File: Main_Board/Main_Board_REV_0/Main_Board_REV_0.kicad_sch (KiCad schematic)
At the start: 24 parts, among them J1 ERF6-30-03.5-L-DV-A-K-TR, J2 ERF6-30-03.5-L-DV-A-K-TR, J3 ERF6-30-03.5-L-DV-A-K-TR, J4 ERF6-30-03.5-L-DV-A-K-TR, J5 ERF6-30-03.5-L-DV-A-K-TR, J6 ERF6-30-03.5-L-DV-A-K-TR, J7 ERF6-30-03.5-L-DV-A-K-TR, J8 ERF6-30-03.5-L-DV-A-K-TR

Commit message: .
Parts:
- added J10, J11, J12, J13, J14, J15, J16, J9: ERF6-30-03.5-L-DV-A-K-TR, 0-lib:SAMTEC_ERF6-30-03.5-L-DV-A-K-TR, symbol 0-lib:ERF6-30-03.5-L-DV-A-K-TR
- H1, H10, H11, H12, H13, H14, H15, H16, H2, H3, H4, H5, H6, H7, H8, H9: footprint MountingHole:MountingHole_2.2mm_M2_DIN965_Pad -> 0-lib:insert
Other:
- note added: "Amplifiers"
- note added: "Cube_1"
- note added: "Cube_2"
- note added: "Cube_3"
- note added: "Cube_4"
- note added: "FARICH"
- note added: "Mounting Inserts"
- title: Fibers Main Board -> Fiber - Main Board
- moved on the sheet: H1, H10, H11, H12, H13, H14, H15, H16, H2, H3, H4, H5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

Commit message: .
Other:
- added sheet Microcontroller (Microcontroller.kicad_sch)
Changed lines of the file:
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@@
+		)
+	)
+	(sheet
+		(at 15.24 438.15)
+		(size 187.96 130.81)
+		(exclude_from_sim no)
+		(in_bom yes)
+		(on_board yes)
+		(dnp no)
+		(stroke
+			(width 1.27)
+			(type solid)
+		)
+		(fill
+			(color 0 0 0 0.0000)
+		)
+		(property "Sheetname" "Microcontroller"
+			(at 66.802 506.222 0)
+			(effects
+				(font
+					(size 7.62 7.62)
+					(thickness 1.524)
+					(bold yes)
+				)
+				(justify left bottom)
+			)
+		)
+		(property "Sheetfile" "Microcontroller.kicad_sch"
+			(at 15.24 569.5446 0)
+			(effects
+				(font
+					(size 1.27 1.27)
+				)
+				(justify left top)
+				(hide yes)
+			)
+		)
+		(instances
+			(project "Main_Board_REV_0"
+				(path "/7125c2d5-be96-492e-8b70-c56cceaf676d"
+					(page "2")
+				)
+			)
 		)
 	)

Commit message: .
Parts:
- added J17: 1778764, 0-lib:PHOENIX_1778764, symbol 0-lib:1778764
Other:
- removed sheet Microcontroller
- moved on the sheet: J1, J10, J11, J12, J13, J14, J15, J16, J2, J3, J4, J5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

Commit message: .
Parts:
- added C1, C10, C11, C12, C13, C14, C15, C16, C17, C18, C19, C2, C20, C3, C4, C5, C6, C7, C8, C9: 10uF, Capacitor_SMD:C_0805_2012Metric, symbol Device:C_Small
- added J18, J20, J21, J22: NCP1117LPST33T3G, Package_TO_SOT_SMD:SOT-223, symbol Connector:Conn_01x03_Pin
- added J19: Conn_02x16_Odd_Even, Connector_PinHeader_2.54mm:PinHeader_2x16_P2.54mm_Vertical, symbol Connector_Generic:Conn_02x16_Odd_Even
- added J23: Amphenol_132289, Connector_Coaxial:SMA_Amphenol_132289_EdgeMount, symbol Connector:Conn_Coaxial_Small
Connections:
- net GND: now also J1.01, J1.03, J1.04, J1.06, J1.08, J1.10, J1.12, J1.13, J1.43, J1.45, J1.50, J1.52, J1.54, J1.56, J1.57, J1.58, J1.59, J1.60, J10.03, J10.04, J10.07, J10.08, J10.11, J10.12, J10.15, J10.16, J10.19, J10.23, J10.24, J10.27, J10.28, J10.31, J10.32, J10.35, J10.36, J10.39, J11.03, J11.04, J11.07, J11.08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
- net Out_D6_Cube_2: now reaches J12.01
- net Out_C8_Cube_2: now reaches J12.02
- net Out_B8_Cube_2: now reaches J12.05
- net Out_D8_Cube_2: now reaches J12.06
- net Out_D7_Cube_2: now reaches J12.09
- net Out_A8_Cube_2: now reaches J12.10
- net Out_C6_Cube_2: now reaches J12.13
- net Out_B7_Cube_2: now reaches J12.14
- net Out_D5_Cube_2: now reaches J12.17
- net Out_C7_Cube_2: now reaches J12.18
- net Out_A7_Cube_2: now reaches J12.21
- net Out_H6_Cube_2: now reaches J12.22
- net Out_A6_Cube_2: now reaches J12.25
- net Out_B5_Cube_2: now reaches J12.26
- net Out_B6_Cube_2: now reaches J12.29
- net Out_B2_Cube_2: now reaches J12.30
- net Out_C5_Cube_2: now reaches J12.33
- net Out_C4_Cube_2: now reaches J12.34
- net Out_C2_Cube_2: now reaches J12.37
- net Out_C3_Cube_2: now reaches J12.38
- net Out_B4_Cube_2: now reaches J12.41
- net Out_A4_Cube_2: now reaches J12.42
- net 1V1_Cube_2: now reaches J12.43
- net 1V1_Cube_2: now also J11.43, J11.44, J11.47, J11.48, J11.51, J11.52, J11.55, J11.56, J12.44, J12.47, J12.48, J12.51, J12.52, J12.55, J12.56
- net Out_D3_Cube_2: now reaches J12.45
- net Out_B3_Cube_2: now reaches J12.46
- net Out_D2_Cube_2: now reaches J12.49
- net Out_A2_Cube_2: now reaches J12.50
- net Out_C1_Cube_2: now reaches J12.53
- net Out_A1_Cube_2: now reaches J12.54
- net Out_B1_Cube_2: now reaches J12.57
- net Out_A3_Cube_2: now reaches J12.58
- net Out_D1_Cube_2: now reaches J12.59
- net Out_D4_Cube_2: now reaches J12.60
- net Out_E8_Cube_1: now reaches J9.01
- net Out_E7_Cube_1: now reaches J9.02
- net Out_H7_Cube_1: now reaches J9.05
- net Out_H8_Cube_1: now reaches J9.06
- net Out_G8_Cube_1: now reaches J9.09
- net Out_F7_Cube_1: now reaches J9.10
- net Out_G7_Cube_1: now reaches J9.13
- net Out_F6_Cube_1: now reaches J9.14
- net Out_F8_Cube_1: now reaches J9.17
- net Out_F5_Cube_1: now reaches J9.18
- net Out_H5_Cube_1: now reaches J9.21
- net Out_E5_Cube_1: now reaches J9.22
- net Out_A5_Cube_1: now reaches J9.25
- net Out_G5_Cube_1: now reaches J9.26
- net Out_G2_Cube_1: now reaches J9.29
- net Out_G6_Cube_1: now reaches J9.30
- net Out_F3_Cube_1: now reaches J9.33
- net Out_E6_Cube_1: now reaches J9.34
- net Out_E4_Cube_1: now reaches J9.37
- net Out_E1_Cube_1: now reaches J9.38
- net Out_H3_Cube_1: now reaches J9.41
- net Out_F4_Cube_1: now reaches J9.42
- net 1V1_Cube_1: now reaches J9.43
- net 1V1_Cube_1: now also J10.43, J10.44, J10.47, J10.48, J10.51, J10.52, J10.55, J10.56, J9.44, J9.47, J9.48, J9.51, J9.52, J9.55, J9.56
- net Out_G4_Cube_1: now reaches J9.45
- net Out_E3_Cube_1: now reaches J9.46
- net Out_H1_Cube_1: now reaches J9.49
- net Out_E2_Cube_1: now reaches J9.50
- net Out_H2_Cube_1: now reaches J9.53
- net Out_G1_Cube_1: now reaches J9.54
- net Out_G3_Cube_1: now reaches J9.57
- net Out_F1_Cube_1: now reaches J9.58
- net Out_H4_Cube_1: now reaches J9.59
- net Out_F2_Cube_1: now reaches J9.60
- net Out_E8_Cube_5: now reaches J13.01
- net Out_E7_Cube_5: now reaches J13.02
- net Out_H7_Cube_5: now reaches J13.05
- net Out_H8_Cube_5: now reaches J13.06
- net Out_G8_Cube_5: now reaches J13.09
- net Out_F7_Cube_5: now reaches J13.10
- net Out_G7_Cube_5: now reaches J13.13
- net Out_F6_Cube_5: now reaches J13.14
- net Out_F8_Cube_5: now reaches J13.17
- net Out_F5_Cube_5: now reaches J13.18
- net Out_H5_Cube_5: now reaches J13.21
- net Out_E5_Cube_5: now reaches J13.22
- net Out_A5_Cube_5: now reaches J13.25
- net Out_G5_Cube_5: now reaches J13.26
- net Out_G2_Cube_5: now reaches J13.29
- net Out_G6_Cube_5: now reaches J13.30
- net Out_F3_Cube_5: now reaches J13.33
- net Out_E6_Cube_5: now reaches J13.34
- net Out_E4_Cube_5: now reaches J13.37
- net Out_E1_Cube_5: now reaches J13.38
- net Out_H3_Cube_5: now reaches J13.41
- net Out_F4_Cube_5: now reaches J13.42
- net 1V1_Cube_5: now reaches J13.43
- net 1V1_Cube_5: now also J13.44, J13.47, J13.48, J13.51, J13.52, J13.55, J13.56, J15.43, J15.44, J15.47, J15.48, J15.51, J15.52, J15.55, J15.56
- net Out_G4_Cube_5: now reaches J13.45
- net Out_E3_Cube_5: now reaches J13.46
- net Out_H1_Cube_5: now reaches J13.49
- net Out_E2_Cube_5: now reaches J13.50
- net Out_H2_Cube_5: now reaches J13.53
- net Out_G1_Cube_5: now reaches J13.54
- net Out_G3_Cube_5: now reaches J13.57
- net Out_F1_Cube_5: now reaches J13.58
- net Out_H4_Cube_5: now reaches J13.59
- net Out_F2_Cube_5: now reaches J13.60
- net 4->5V: now reaches J17.1
- net 4->5V: now also C11.2, C14.2, C16.2, C2.1, C3.1, C5.1, C7.1, C9.2, J18.3 (Pin_3), J19.1 (Pin_1), J19.2 (Pin_2), J20.3 (Pin_3), J21.3 (Pin_3), J22.3 (Pin_3)
- net at J2.06: now also J2.08, J2.10, J2.12, J2.14
- net Ch_61_A1: now reaches J2.13
- net Ch_63_A1: now reaches J2.15
- net Ch_55_A1: now reaches J2.17
- net Ch_57_A1: now reaches J2.19
- net Ch_59_A1: now reaches J2.20
- net Ch_47_A1: now reaches J2.21
- net Ch_51_A1: now reaches J2.22
- net Ch_53_A1: now reaches J2.23
- net Ch_49_A1: now reaches J2.24
- net Ch_37_A1: now reaches J2.25
- net Ch_45_A1: now reaches J2.26
- net Ch_43_A1: now reaches J2.27
- net Ch_41_A1: now reaches J2.28
- net Ch_27_A1: now reaches J2.29
- net Ch_39_A1: now reaches J2.30
- net Ch_33_A1: now reaches J2.31
- net Ch_35_A1: now reaches J2.32
- net Ch_17_A1: now reaches J2.33
- net Ch_31_A1: now reaches J2.34
- net Ch_23_A1: now reaches J2.35
- net Ch_29_A1: now reaches J2.36
- net Ch_11_A1: now reaches J2.37
- net Ch_25_A1: now reaches J2.38
- net Ch_15_A1: now reaches J2.39
- net Ch_21_A1: now reaches J2.40
- net Ch_07_A1: now reaches J2.41
- net Ch_19_A1: now reaches J2.42
- net Ch_09_A1: now reaches J2.43
- net Ch_13_A1: now reaches J2.44
- net Ch_01_A1: now reaches J2.45
- net Ch_05_A1: now reaches J2.46
- net Ch_03_A1: now reaches J2.47
- net 1V1_A1: now reaches J2.50
- net 1V1_A1: now also J1.05, J1.07, J1.09, J1.11, J2.52, J2.54, J2.56
- net HV_1-32_A1: now reaches J2.59
- net HV_1-32_A1: now also J19.32 (Pin_32)
- net at J8.06: now also J8.08, J8.10, J8.12, J8.14
- net Ch_61_A4: now reaches J8.13
- net Ch_63_A4: now reaches J8.15
- net Ch_55_A4: now reaches J8.17
- net Ch_57_A4: now reaches J8.19
- net Ch_59_A4: now reaches J8.20
- net Ch_47_A4: now reaches J8.21
- net Ch_51_A4: now reaches J8.22
- net Ch_53_A4: now reaches J8.23
- net Ch_49_A4: now reaches J8.24
- net Ch_37_A4: now reaches J8.25
- net Ch_45_A4: now reaches J8.26
- net Ch_43_A4: now reaches J8.27
- net Ch_41_A4: now reaches J8.28
- net Ch_27_A4: now reaches J8.29
- net Ch_39_A4: now reaches J8.30
- net Ch_33_A4: now reaches J8.31
- net Ch_35_A4: now reaches J8.32
- net Ch_17_A4: now reaches J8.33
- net Ch_31_A4: now reaches J8.34
- net Ch_23_A4: now reaches J8.35
- net Ch_29_A4: now reaches J8.36
- net Ch_11_A4: now reaches J8.37
- net Ch_25_A4: now reaches J8.38
- net Ch_15_A4: now reaches J8.39
- net Ch_21_A4: now reaches J8.40
- net Ch_07_A4: now reaches J8.41
- net Ch_19_A4: now reaches J8.42
- net Ch_09_A4: now reaches J8.43
- net Ch_13_A4: now reaches J8.44
- net Ch_01_A4: now reaches J8.45
- net Ch_05_A4: now reaches J8.46
- net Ch_03_A4: now reaches J8.47
- net 1V1_A4: now reaches J8.50
- net 1V1_A4: now also J7.05, J7.07, J7.09, J7.11, J8.52, J8.54, J8.56
- net HV_1-32_A4: now reaches J8.59
- net HV_1-32_A4: now also J19.26 (Pin_26)
- net at J4.06: now also J4.08, J4.10, J4.12, J4.14
- net Ch_61_A2: now reaches J4.13
- net Ch_63_A2: now reaches J4.15
- net Ch_55_A2: now reaches J4.17
- net Ch_57_A2: now reaches J4.19
- net Ch_59_A2: now reaches J4.20
- net Ch_47_A2: now reaches J4.21
- net Ch_51_A2: now reaches J4.22
- net Ch_53_A2: now reaches J4.23
- net Ch_49_A2: now reaches J4.24
- net Ch_37_A2: now reaches J4.25
- net Ch_45_A2: now reaches J4.26
- net Ch_43_A2: now reaches J4.27
- net Ch_41_A2: now reaches J4.28
- net Ch_27_A2: now reaches J4.29
- net Ch_39_A2: now reaches J4.30
- net Ch_33_A2: now reaches J4.31
- net Ch_35_A2: now reaches J4.32
- net Ch_17_A2: now reaches J4.33
- net Ch_31_A2: now reaches J4.34
- net Ch_23_A2: now reaches J4.35
- net Ch_29_A2: now reaches J4.36
- net Ch_11_A2: now reaches J4.37
- net Ch_25_A2: now reaches J4.38
- net Ch_15_A2: now reaches J4.39
- net Ch_21_A2: now reaches J4.40
- net Ch_07_A2: now reaches J4.41
- net Ch_19_A2: now reaches J4.42
- net Ch_09_A2: now reaches J4.43
- net Ch_13_A2: now reaches J4.44
- net Ch_01_A2: now reaches J4.45
- net Ch_05_A2: now reaches J4.46
- net Ch_03_A2: now reaches J4.47
- net 1V1_A2: now reaches J4.50
- net 1V1_A2: now also J3.05, J3.07, J3.09, J3.11, J4.52, J4.54, J4.56
- net HV_1-32_A2: now reaches J4.59
- net HV_1-32_A2: now also J19.30 (Pin_30)
- net HV_33-64_A2: now reaches J3.02
- net HV_33-64_A2: now also J19.20 (Pin_20)
- net Ch_62_A2: now reaches J3.14
- net Ch_60_A2: now reaches J3.15
- net Ch_64_A2: now reaches J3.16
- net Ch_54_A2: now reaches J3.17
- net Ch_56_A2: now reaches J3.18
- net Ch_48_A2: now reaches J3.19
- net Ch_58_A2: now reaches J3.20
- net Ch_44_A2: now reaches J3.21
- net Ch_50_A2: now reaches J3.22
- net Ch_40_A2: now reaches J3.23
- net Ch_52_A2: now reaches J3.24
- net Ch_36_A2: now reaches J3.25
- net Ch_42_A2: now reaches J3.26
- net Ch_34_A2: now reaches J3.27
- net Ch_46_A2: now reaches J3.28
- net Ch_30_A2: now reaches J3.29
- net Ch_32_A2: now reaches J3.30
- net Ch_26_A2: now reaches J3.31
- net Ch_38_A2: now reaches J3.32
- net Ch_24_A2: now reaches J3.33
- net Ch_22_A2: now reaches J3.34
- net Ch_20_A2: now reaches J3.35
- net Ch_28_A2: now reaches J3.36
- net Ch_16_A2: now reaches J3.37
- net Ch_12_A2: now reaches J3.38
- net Ch_14_A2: now reaches J3.39
- net Ch_18_A2: now reaches J3.40
- net Ch_08_A2: now reaches J3.41
- net Ch_06_A2: now reaches J3.42
- net Ch_10_A2: now reaches J3.44
- net Ch_02_A2: now reaches J3.46
- net +3.3_2V: now reaches J3.47
- net +3.3_2V: now also J3.49, J3.51, J3.53, J3.55, C15.1, C18.1, C6.1, J21.2 (Pin_2)
- net Ch_04_A2: now reaches J3.48
- net Out_D6_Cube_1: now reaches J10.01
- net Out_C8_Cube_1: now reaches J10.02
- net Out_B8_Cube_1: now reaches J10.05
- net Out_D8_Cube_1: now reaches J10.06
- net Out_D7_Cube_1: now reaches J10.09
- net Out_A8_Cube_1: now reaches J10.10
- net Out_C6_Cube_1: now reaches J10.13
- net Out_B7_Cube_1: now reaches J10.14
- net Out_D5_Cube_1: now reaches J10.17
- net Out_C7_Cube_1: now reaches J10.18
- net Out_A7_Cube_1: now reaches J10.21
- net Out_H6_Cube_1: now reaches J10.22
- net Out_A6_Cube_1: now reaches J10.25
- net Out_B5_Cube_1: now reaches J10.26
- net Out_B6_Cube_1: now reaches J10.29
- net Out_B2_Cube_1: now reaches J10.30
- net Out_C5_Cube_1: now reaches J10.33
- net Out_C4_Cube_1: now reaches J10.34
- net Out_C2_Cube_1: now reaches J10.37
- net Out_C3_Cube_1: now reaches J10.38
- net Out_B4_Cube_1: now reaches J10.41
- net Out_A4_Cube_1: now reaches J10.42
- net Out_D3_Cube_1: now reaches J10.45
- net Out_B3_Cube_1: now reaches J10.46
- net Out_D2_Cube_1: now reaches J10.49
- net Out_A2_Cube_1: now reaches J10.50
- net Out_C1_Cube_1: now reaches J10.53
- net Out_A1_Cube_1: now reaches J10.54
- net Out_B1_Cube_1: now reaches J10.57
- net Out_A3_Cube_1: now reaches J10.58
- net Out_D1_Cube_1: now reaches J10.59
- net Out_D4_Cube_1: now reaches J10.60
- net HV_33-64_A3: now reaches J5.02
- net HV_33-64_A3: now also J19.22 (Pin_22)
- net 1V1_A3: now reaches J5.05
- net 1V1_A3: now also J5.07, J5.09, J5.11, J6.50, J6.52, J6.54, J6.56
- net Ch_62_A3: now reaches J5.14
- net Ch_60_A3: now reaches J5.15
- net Ch_64_A3: now reaches J5.16
- net Ch_54_A3: now reaches J5.17
- net Ch_56_A3: now reaches J5.18
- net Ch_48_A3: now reaches J5.19
- net Ch_58_A3: now reaches J5.20
- net Ch_44_A3: now reaches J5.21
- net Ch_50_A3: now reaches J5.22
- net Ch_40_A3: now reaches J5.23
- net Ch_52_A3: now reaches J5.24
- net Ch_36_A3: now reaches J5.25
- net Ch_42_A3: now reaches J5.26
- net Ch_34_A3: now reaches J5.27
- net Ch_46_A3: now reaches J5.28
- net Ch_30_A3: now reaches J5.29
- net Ch_32_A3: now reaches J5.30
- net Ch_26_A3: now reaches J5.31
- net Ch_38_A3: now reaches J5.32
- net Ch_24_A3: now reaches J5.33
- net Ch_22_A3: now reaches J5.34
- net Ch_20_A3: now reaches J5.35
- net Ch_28_A3: now reaches J5.36
- net Ch_16_A3: now reaches J5.37
- net Ch_12_A3: now reaches J5.38
- net Ch_14_A3: now reaches J5.39
- net Ch_18_A3: now reaches J5.40
- net Ch_08_A3: now reaches J5.41
- net Ch_06_A3: now reaches J5.42
- net Ch_10_A3: now reaches J5.44
- net Ch_02_A3: now reaches J5.46
- net +3.3_3V: now reaches J5.47
- net +3.3_3V: now also J5.49, J5.51, J5.53, J5.55, C12.1, C19.1, C4.1, J20.2 (Pin_2)
- net Ch_04_A3: now reaches J5.48
- net Out_D6_Cube_5: now reaches J15.01
- net Out_C8_Cube_5: now reaches J15.02
- net Out_B8_Cube_5: now reaches J15.05
- net Out_D8_Cube_5: now reaches J15.06
- net Out_D7_Cube_5: now reaches J15.09
- net Out_A8_Cube_5: now reaches J15.10
- net Out_C6_Cube_5: now reaches J15.13
- net Out_B7_Cube_5: now reaches J15.14
- net Out_D5_Cube_5: now reaches J15.17
- net Out_C7_Cube_5: now reaches J15.18
- net Out_A7_Cube_5: now reaches J15.21
- net Out_H6_Cube_5: now reaches J15.22
- net Out_A6_Cube_5: now reaches J15.25
- net Out_B5_Cube_5: now reaches J15.26
- net Out_B6_Cube_5: now reaches J15.29
- net Out_B2_Cube_5: now reaches J15.30
- net Out_C5_Cube_5: now reaches J15.33
- net Out_C4_Cube_5: now reaches J15.34
- net Out_C2_Cube_5: now reaches J15.37
- net Out_C3_Cube_5: now reaches J15.38
- net Out_B4_Cube_5: now reaches J15.41
- net Out_A4_Cube_5: now reaches J15.42
- net Out_D3_Cube_5: now reaches J15.45
- net Out_B3_Cube_5: now reaches J15.46
- net Out_D2_Cube_5: now reaches J15.49
- net Out_A2_Cube_5: now reaches J15.50
- net Out_C1_Cube_5: now reaches J15.53
- net Out_A1_Cube_5: now reaches J15.54
- net Out_B1_Cube_5: now reaches J15.57
- net Out_A3_Cube_5: now reaches J15.58
- net Out_D1_Cube_5: now reaches J15.59
- net Out_D4_Cube_5: now reaches J15.60
- net Out_D6_Cube_6: now reaches J16.01
- net Out_C8_Cube_6: now reaches J16.02
- net Out_B8_Cube_6: now reaches J16.05
- net Out_D8_Cube_6: now reaches J16.06
- net Out_D7_Cube_6: now reaches J16.09
- net Out_A8_Cube_6: now reaches J16.10
- net Out_C6_Cube_6: now reaches J16.13
- net Out_B7_Cube_6: now reaches J16.14
- net Out_D5_Cube_6: now reaches J16.17
- net Out_C7_Cube_6: now reaches J16.18
- net Out_A7_Cube_6: now reaches J16.21
- net Out_H6_Cube_6: now reaches J16.22
- net Out_A6_Cube_6: now reaches J16.25
- net Out_B5_Cube_6: now reaches J16.26
- net Out_B6_Cube_6: now reaches J16.29
- net Out_B2_Cube_6: now reaches J16.30
- net Out_C5_Cube_6: now reaches J16.33
- net Out_C4_Cube_6: now reaches J16.34
- net Out_C2_Cube_6: now reaches J16.37
- net Out_C3_Cube_6: now reaches J16.38
- net Out_B4_Cube_6: now reaches J16.41
- net Out_A4_Cube_6: now reaches J16.42
- net 1V1_Cube_6: now reaches J16.43
- net 1V1_Cube_6: now also J14.43, J14.44, J14.47, J14.48, J14.51, J14.52, J14.55, J14.56, J16.44, J16.47, J16.48, J16.51, J16.52, J16.55, J16.56
- net Out_D3_Cube_6: now reaches J16.45
- net Out_B3_Cube_6: now reaches J16.46
- net Out_D2_Cube_6: now reaches J16.49
- net Out_A2_Cube_6: now reaches J16.50
- net Out_C1_Cube_6: now reaches J16.53
- net Out_A1_Cube_6: now reaches J16.54
- net Out_B1_Cube_6: now reaches J16.57
- net Out_A3_Cube_6: now reaches J16.58
- net Out_D1_Cube_6: now reaches J16.59
- net Out_D4_Cube_6: now reaches J16.60
- net HV_33-64_A4: now reaches J7.02
- net HV_33-64_A4: now also J19.24 (Pin_24)
- net Ch_62_A4: now reaches J7.14
- net Ch_60_A4: now reaches J7.15
- net Ch_64_A4: now reaches J7.16
- net Ch_54_A4: now reaches J7.17
- net Ch_56_A4: now reaches J7.18
- net Ch_48_A4: now reaches J7.19
- net Ch_58_A4: now reaches J7.20
- net Ch_44_A4: now reaches J7.21
- net Ch_50_A4: now reaches J7.22
- net Ch_40_A4: now reaches J7.23
- net Ch_52_A4: now reaches J7.24
- net Ch_36_A4: now reaches J7.25
- net Ch_42_A4: now reaches J7.26
- net Ch_34_A4: now reaches J7.27
- net Ch_46_A4: now reaches J7.28
- net Ch_30_A4: now reaches J7.29
- net Ch_32_A4: now reaches J7.30
- net Ch_26_A4: now reaches J7.31
- net Ch_38_A4: now reaches J7.32
- net Ch_24_A4: now reaches J7.33
- net Ch_22_A4: now reaches J7.34
- net Ch_20_A4: now reaches J7.35
- net Ch_28_A4: now reaches J7.36
- net Ch_16_A4: now reaches J7.37
- net Ch_12_A4: now reaches J7.38
- net Ch_14_A4: now reaches J7.39
- net Ch_18_A4: now reaches J7.40
- net Ch_08_A4: now reaches J7.41
- net Ch_06_A4: now reaches J7.42
- net Ch_10_A4: now reaches J7.44
- net Ch_02_A4: now reaches J7.46
- net +3.3_4V: now reaches J7.47
- net +3.3_4V: now also J7.49, J7.51, J7.53, J7.55, C13.1, C20.1, C8.1, J22.2 (Pin_2)
- net Ch_04_A4: now reaches J7.48
- net HV_33-64_A1: now reaches J1.02
- net HV_33-64_A1: now also J19.18 (Pin_18)
- net Ch_62_A1: now reaches J1.14
- net Ch_60_A1: now reaches J1.15
- net Ch_64_A1: now reaches J1.16
- net Ch_54_A1: now reaches J1.17
- net Ch_56_A1: now reaches J1.18
- net Ch_48_A1: now reaches J1.19
- net Ch_58_A1: now reaches J1.20
- net Ch_44_A1: now reaches J1.21
- net Ch_50_A1: now reaches J1.22
- net Ch_40_A1: now reaches J1.23
- net Ch_52_A1: now reaches J1.24
- net Ch_36_A1: now reaches J1.25
- net Ch_42_A1: now reaches J1.26
- net Ch_34_A1: now reaches J1.27
- net Ch_46_A1: now reaches J1.28
- net Ch_30_A1: now reaches J1.29
- net Ch_32_A1: now reaches J1.30
- net Ch_26_A1: now reaches J1.31
- net Ch_38_A1: now reaches J1.32
- net Ch_24_A1: now reaches J1.33
- net Ch_22_A1: now reaches J1.34
- net Ch_20_A1: now reaches J1.35
- net Ch_28_A1: now reaches J1.36
- net Ch_16_A1: now reaches J1.37
- net Ch_12_A1: now reaches J1.38
- net Ch_14_A1: now reaches J1.39
- net Ch_18_A1: now reaches J1.40
- net Ch_08_A1: now reaches J1.41
- net Ch_06_A1: now reaches J1.42
- net Ch_10_A1: now reaches J1.44
- net Ch_02_A1: now reaches J1.46
- net +3.3_1V: now reaches J1.47
- net +3.3_1V: now also J1.49, J1.51, J1.53, J1.55, C1.1, C10.1, C17.1, J18.2 (Pin_2)
- net Ch_04_A1: now reaches J1.48
- net Out_E8_Cube_2: now reaches J11.01
- net Out_E7_Cube_2: now reaches J11.02
- net Out_H7_Cube_2: now reaches J11.05
- net Out_H8_Cube_2: now reaches J11.06
- net Out_G8_Cube_2: now reaches J11.09
- net Out_F7_Cube_2: now reaches J11.10
- net Out_G7_Cube_2: now reaches J11.13
- net Out_F6_Cube_2: now reaches J11.14
- net Out_F8_Cube_2: now reaches J11.17
- net Out_F5_Cube_2: now reaches J11.18
- net Out_H5_Cube_2: now reaches J11.21
- net Out_E5_Cube_2: now reaches J11.22
- net Out_A5_Cube_2: now reaches J11.25
- net Out_G5_Cube_2: now reaches J11.26
- net Out_G2_Cube_2: now reaches J11.29
- net Out_G6_Cube_2: now reaches J11.30
- net Out_F3_Cube_2: now reaches J11.33
- net Out_E6_Cube_2: now reaches J11.34
- net Out_E4_Cube_2: now reaches J11.37
- net Out_E1_Cube_2: now reaches J11.38
- net Out_H3_Cube_2: now reaches J11.41
- net Out_F4_Cube_2: now reaches J11.42
- net Out_G4_Cube_2: now reaches J11.45
- net Out_E3_Cube_2: now reaches J11.46
- net Out_H1_Cube_2: now reaches J11.49
- net Out_E2_Cube_2: now reaches J11.50
- net Out_H2_Cube_2: now reaches J11.53
- net Out_G1_Cube_2: now reaches J11.54
- net Out_G3_Cube_2: now reaches J11.57
- net Out_F1_Cube_2: now reaches J11.58
- net Out_H4_Cube_2: now reaches J11.59
- net Out_F2_Cube_2: now reaches J11.60
- net at J6.06: now also J6.08, J6.10, J6.12, J6.14
- net Ch_61_A3: now reaches J6.13
- net Ch_63_A3: now reaches J6.15
- net Ch_55_A3: now reaches J6.17
- net Ch_57_A3: now reaches J6.19
- net Ch_59_A3: now reaches J6.20
- net Ch_47_A3: now reaches J6.21
- net Ch_51_A3: now reaches J6.22
- net Ch_53_A3: now reaches J6.23
- net Ch_49_A3: now reaches J6.24
- net Ch_37_A3: now reaches J6.25
- net Ch_45_A3: now reaches J6.26
- net Ch_43_A3: now reaches J6.27
- net Ch_41_A3: now reaches J6.28
- net Ch_27_A3: now reaches J6.29
- net Ch_39_A3: now reaches J6.30
- net Ch_33_A3: now reaches J6.31
- net Ch_35_A3: now reaches J6.32
- net Ch_17_A3: now reaches J6.33
- net Ch_31_A3: now reaches J6.34
- net Ch_23_A3: now reaches J6.35
- net Ch_29_A3: now reaches J6.36
- net Ch_11_A3: now reaches J6.37
- net Ch_25_A3: now reaches J6.38
- net Ch_15_A3: now reaches J6.39
- net Ch_21_A3: now reaches J6.40
- net Ch_07_A3: now reaches J6.41
- net Ch_19_A3: now reaches J6.42
- net Ch_09_A3: now reaches J6.43
- net Ch_13_A3: now reaches J6.44
- net Ch_01_A3: now reaches J6.45
- net Ch_05_A3: now reaches J6.46
- net Ch_03_A3: now reaches J6.47
- net HV_1-32_A3: now reaches J6.59
- net HV_1-32_A3: now also J19.28 (Pin_28)
- net Out_E8_Cube_6: now reaches J14.01
- net Out_E7_Cube_6: now reaches J14.02
- net Out_H7_Cube_6: now reaches J14.05
- net Out_H8_Cube_6: now reaches J14.06
- net Out_G8_Cube_6: now reaches J14.09
- net Out_F7_Cube_6: now reaches J14.10
- net Out_G7_Cube_6: now reaches J14.13
- net Out_F6_Cube_6: now reaches J14.14
- net Out_F8_Cube_6: now reaches J14.17
- net Out_F5_Cube_6: now reaches J14.18
- net Out_H5_Cube_6: now reaches J14.21
- net Out_E5_Cube_6: now reaches J14.22
- net Out_A5_Cube_6: now reaches J14.25
- net Out_G5_Cube_6: now reaches J14.26
- net Out_G2_Cube_6: now reaches J14.29
- net Out_G6_Cube_6: now reaches J14.30
- net Out_F3_Cube_6: now reaches J14.33
- net Out_E6_Cube_6: now reaches J14.34
- net Out_E4_Cube_6: now reaches J14.37
- net Out_E1_Cube_6: now reaches J14.38
- net Out_H3_Cube_6: now reaches J14.41
- net Out_F4_Cube_6: now reaches J14.42
- net Out_G4_Cube_6: now reaches J14.45
- net Out_E3_Cube_6: now reaches J14.46
- net Out_H1_Cube_6: now reaches J14.49
- net Out_E2_Cube_6: now reaches J14.50
- net Out_H2_Cube_6: now reaches J14.53
- net Out_G1_Cube_6: now reaches J14.54
- net Out_G3_Cube_6: now reaches J14.57
- net Out_F1_Cube_6: now reaches J14.58
- net Out_H4_Cube_6: now reaches J14.59
- net Out_F2_Cube_6: now reaches J14.60
- new net HV_In: J19.17 (Pin_17), J19.19 (Pin_19), J19.21 (Pin_21), J19.23 (Pin_23), J19.25 (Pin_25), J19.27 (Pin_27), J19.29 (Pin_29), J19.31 (Pin_31), J23.1 (In)
- no-connect marks 0 -> 20
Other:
- note added: "3.3V for Amp."
- note added: "Amp_1"
- note added: "Amp_2"
- note added: "Amp_3"
- note added: "Amp_4"
- note added: "Cube_3 not in use!"
- note added: "Cube_4 not in use!"
- note added: "Cube_5"
- note added: "Cube_6"
- moved on the sheet: J1, J10, J17, J2, J9

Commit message: Update PCB and schematic; refresh backups
Removed outdated backup files and added new backups for Main_Board_REV_0. Updated the PCB file and schematic with new labels for Cube 2 outputs and changed high contrast mode in the project layout. Minor binary change in SmallFiber/.DS_Store.
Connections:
- net Out_E1_Cube_2 is gone; now on net Ch_34_A1: J11.38
- net Out_E2_Cube_2 is gone; now on net Ch_44_A1: J11.50
- net Out_E3_Cube_2 is gone; now on net Ch_40_A1: J11.46
- net Out_E4_Cube_2 is gone; now on net Ch_08_A1: J11.37
- net Out_F1_Cube_2 is gone; now on net Ch_54_A1: J11.58
- net Out_F2_Cube_2 is gone; now on net Ch_60_A1: J11.60
- net Out_F4_Cube_2 is gone; now on net Ch_36_A1: J11.42
- net Out_G1_Cube_2 is gone; now on net Ch_48_A1: J11.54
- net Out_G3_Cube_2 is gone; now on net Ch_26_A1: J11.57
- net Out_G4_Cube_2 is gone; now on net Ch_16_A1: J11.45
- net Out_H1_Cube_2 is gone; now on net Ch_20_A1: J11.49
- net Out_H2_Cube_2 is gone; now on net Ch_24_A1: J11.53
- net Out_H3_Cube_2 is gone; now on net Ch_14_A1: J11.41
- net Out_H4_Cube_2 is gone; now on net Ch_30_A1: J11.59
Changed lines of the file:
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@@
 		)
 	)
+	(label "Out_E2_Cube_2"
+		(at 29.21 64.77 0)
+		(effects
+			(font
+				(size 1.27 1.27)
+			)
+			(justify left bottom)
+		)
+	)
 	(label "Out_B5_Cube_1"
 		(at 175.26 353.06 0)
@@
 		)
 	)
+	(label "Out_E3_Cube_2"
+		(at 29.21 67.31 0)
+		(effects
+			(font
+				(size 1.27 1.27)
+			)
+			(justify left bottom)
+		)
+	)
 	(label "Out_E8_Cube_5"
 		(at 421.64 325.12 180)
@@
 		)
 	)
+	(label "Out_G4_Cube_2"
+		(at 29.21 85.09 0)
+		(effects
+			(font
+				(size 1.27 1.27)
+			)
+			(justify left bottom)
+		)
+	)
 	(label "Out_A1_Cube_6"
 		(at 510.54 265.43 0)
@@
 		)
 	)
+	(label "Out_H2_Cube_2"
+		(at 29.21 80.01 0)
+		(effects
+			(font
+				(size 1.27 1.27)
+			)
+			(justify left bottom)
+		)
+	)
 	(label "GND"
 		(at 483.87 207.01 180)
@@
 		)
 	)
+	(label "Out_H1_Cube_2"
+		(at 29.21 82.55 0)
+		(effects
+			(font
+				(size 1.27 1.27)
+			)
+			(justify left bottom)
+		)
+	)
 	(label "Out_D5_Cube_1"
 		(at 148.59 342.9 180)
@@
 		)
 	)
+	(label "Out_G3_Cube_2"
+		(at 29.21 77.47 0)
+		(effects
+			(font
+				(size 1.27 1.27)
+			)
+			(justify left bottom)
+		)
+	)
 	(label "Out_B2_Cube_6"
 		(at 510.54 234.95 0)
@@
 		)
 	)
+	(label "Out_G1_Cube_2"
+		(at 29.21 62.23 0)
+		(effects
+			(font
+				(size 1.27 1.27)
+			)
+			(justify left bottom)
+		)
+	)
 	(label "Out_D6_Cube_6"
 		(at 483.87 199.39 180)
@@
 		)
 	)
+	(label "Out_H4_Cube_2"
+		(at 29.21 74.93 0)
+		(effects
+			(font
+				(size 1.27 1.27)
+			)
+			(justify left bottom)
+		)
+	)
 	(label "Out_A7_Cube_2"
 		(at 148.59 219.71 180)
@@
 		)
 	)
+	(label "Out_F1_Cube_2"
+		(at 29.21 59.69 0)
+		(effects
+			(font
+				(size 1.27 1.27)
+			)
+			(justify left bottom)
+		)
+	)
 	(label "1V1_Cube_6"
 		(at 510.54 252.73 0)
@@
 		)
 	)
+	(label "Out_E1_Cube_2"
+		(at 29.21 72.39 0)
+		(effects
+			(font
+				(size 1.27 1.27)
+			)
+			(justify left bottom)
+		)
+	)
 	(label "Out_H7_Cube_1"
 		(at 85.09 327.66 180)
@@
 		)
 	)
+	(label "Out_H3_Cube_2"
+		(at 29.21 87.63 0)
+		(effects
+			(font
+				(size 1.27 1.27)
+			)
+			(justify left bottom)
+		)
+	)
 	(label "Out_B5_Cube_6"
 		(at 510.54 229.87 0)
@@
 		)
 	)
+	(label "Out_E4_Cube_2"
+		(at 29.21 90.17 0)
+		(effects
+			(font
+				(size 1.27 1.27)
+			)
+			(justify left bottom)
+		)
+	)
 	(label "Out_F6_Cube_2"
 		(at 114.3 209.55 0)
@@
 		)
 	)
+	(label "Out_F2_Cube_2"
+		(at 29.21 57.15 0)
+		(effects
+			(font
+				(size 1.27 1.27)
+			)
+			(justify left bottom)
+		)
+	)
 	(label "Out_C2_Cube_6"
 		(at 483.87 245.11 180)
@@
 		(effects
 			(font
+				(size 1.27 1.27)
+			)
+			(justify left bottom)
+		)
+	)
+	(label "Out_F4_Cube_2"
+		(at 29.21 69.85 0)
+		(effects
+			(font

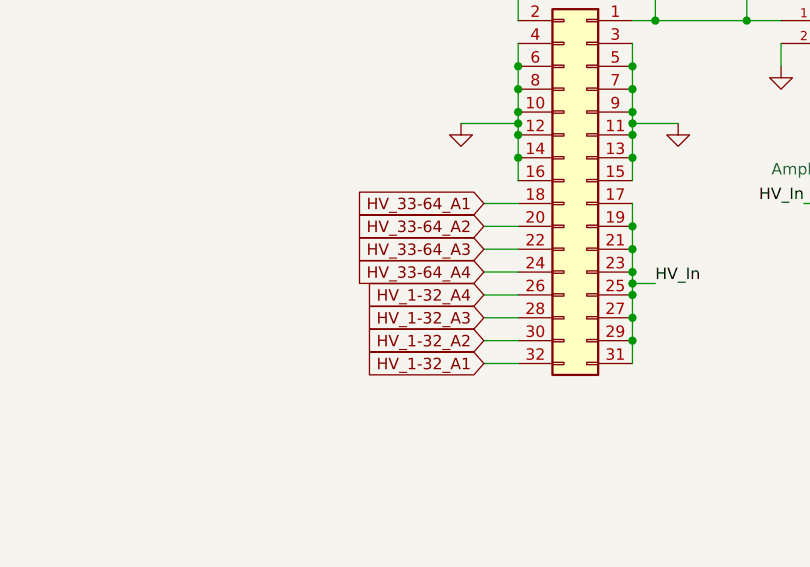
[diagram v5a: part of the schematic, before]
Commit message: Update PCB and schematic, add net colors and track width
Updated KiCad PCB and schematic files with changes to global label positions and net assignments. Added custom net colors and an additional track width in the project file. Adjusted project settings for net color mode and high contrast mode. Backup files were updated to reflect the latest project state.
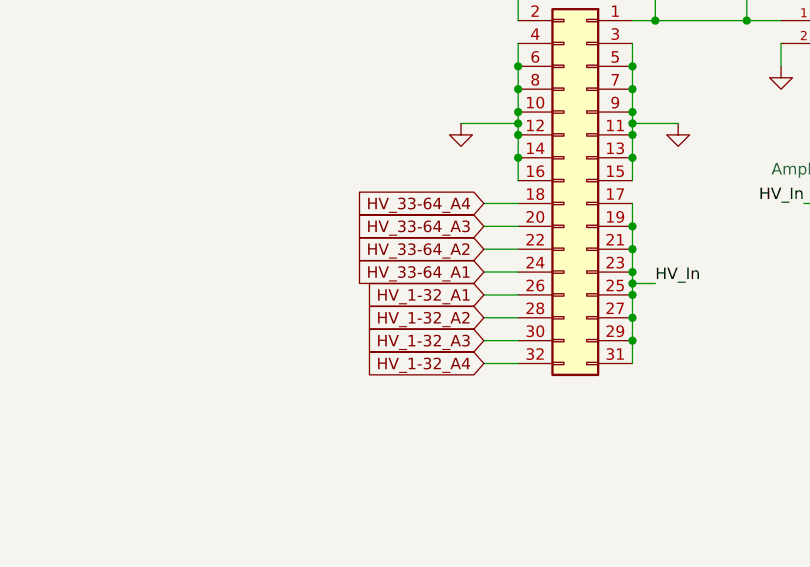
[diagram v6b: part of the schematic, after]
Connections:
- net HV_1-32_A1: now also J19.26 (Pin_26); no longer J19.32 (Pin_32)
- net HV_1-32_A2: now also J19.28 (Pin_28); no longer J19.30 (Pin_30)
- net HV_1-32_A3: now also J19.30 (Pin_30); no longer J19.28 (Pin_28)
- net HV_1-32_A4: now also J19.32 (Pin_32); no longer J19.26 (Pin_26)
- net HV_33-64_A1: now also J19.24 (Pin_24); no longer J19.18 (Pin_18)
- net HV_33-64_A2: now also J19.22 (Pin_22); no longer J19.20 (Pin_20)
- net HV_33-64_A3: now also J19.20 (Pin_20); no longer J19.22 (Pin_22)
- net HV_33-64_A4: now also J19.18 (Pin_18); no longer J19.24 (Pin_24)
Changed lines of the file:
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@@
 	(global_label "HV_33-64_A2"
 		(shape input)
-		(at 749.3 269.24 180)
+		(at 749.3 271.78 180)
 		(fields_autoplaced yes)
 		(effects
@@
 		)
 		(property "Intersheetrefs" "${INTERSHEET_REFS}"
-			(at 733.252 269.24 0)
+			(at 733.252 271.78 0)
 			(effects
 				(font
@@
 	(global_label "HV_1-32_A3"
 		(shape input)
-		(at 749.3 279.4 180)
+		(at 749.3 281.94 180)
 		(fields_autoplaced yes)
 		(effects
@@
 		)
 		(property "Intersheetrefs" "${INTERSHEET_REFS}"
-			(at 734.4615 279.4 0)
+			(at 734.4615 281.94 0)
 			(effects
 				(font
@@
 	(global_label "HV_1-32_A1"
 		(shape input)
-		(at 749.3 284.48 180)
+		(at 749.3 276.86 180)
 		(fields_autoplaced yes)
 		(effects
@@
 		)
 		(property "Intersheetrefs" "${INTERSHEET_REFS}"
-			(at 734.4615 284.48 0)
+			(at 734.4615 276.86 0)
 			(effects
 				(font
@@
 	(global_label "HV_1-32_A4"
 		(shape input)
-		(at 749.3 276.86 180)
+		(at 749.3 284.48 180)
 		(fields_autoplaced yes)
 		(effects
@@
 		)
 		(property "Intersheetrefs" "${INTERSHEET_REFS}"
-			(at 734.4615 276.86 0)
+			(at 734.4615 284.48 0)
 			(effects
 				(font
@@
 	(global_label "HV_1-32_A2"
 		(shape input)
-		(at 749.3 281.94 180)
+		(at 749.3 279.4 180)
 		(fields_autoplaced yes)
 		(effects
@@
 		)
 		(property "Intersheetrefs" "${INTERSHEET_REFS}"
-			(at 734.4615 281.94 0)
+			(at 734.4615 279.4 0)
 			(effects
 				(font
@@
 	(global_label "HV_33-64_A4"
 		(shape input)
-		(at 749.3 274.32 180)
+		(at 749.3 266.7 180)
 		(fields_autoplaced yes)
 		(effects
@@
 		)
 		(property "Intersheetrefs" "${INTERSHEET_REFS}"
-			(at 733.252 274.32 0)
+			(at 733.252 266.7 0)
 			(effects
 				(font
@@
 	(global_label "HV_33-64_A3"
 		(shape input)
-		(at 749.3 271.78 180)
+		(at 749.3 269.24 180)
 		(fields_autoplaced yes)
 		(effects
@@
 		)
 		(property "Intersheetrefs" "${INTERSHEET_REFS}"
-			(at 733.252 271.78 0)
+			(at 733.252 269.24 0)
 			(effects
 				(font
@@
 	(global_label "HV_33-64_A1"
 		(shape input)
-		(at 749.3 266.7 180)
+		(at 749.3 274.32 180)
 		(fields_autoplaced yes)
 		(effects
@@
 		)
 		(property "Intersheetrefs" "${INTERSHEET_REFS}"
-			(at 733.252 266.7 0)
+			(at 733.252 274.32 0)
 			(effects
 				(font

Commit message: Update Main Board schematic and PCB, add backups
Added new backup ZIP files for HV_MPPC_Ballance_prototype and Main_Board_REV_0, and removed outdated backups. Updated Main_Board_REV_0 KiCad project: reduced net class clearance, enabled high contrast mode, added a TestPoint symbol, and made significant schematic wiring and connection changes.
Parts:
- added TP1: 1V1_A1, TestPoint:TestPoint_Pad_1.0x1.0mm, symbol Connector:TestPoint
- added TP2: 3V3_A1, TestPoint:TestPoint_Pad_1.0x1.0mm, symbol Connector:TestPoint
- added TP3: 3V3_A2, TestPoint:TestPoint_Pad_1.0x1.0mm, symbol Connector:TestPoint
- added TP4: 3V3_A3, TestPoint:TestPoint_Pad_1.0x1.0mm, symbol Connector:TestPoint
- added TP5: 3V3_A4, TestPoint:TestPoint_Pad_1.0x1.0mm, symbol Connector:TestPoint
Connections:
- net 1V1_Cube_2 is gone; now on net 1V1_A1: J11.43, J11.44, J11.47, J11.48, J11.51, J11.52, J11.55, J11.56, J12.43, J12.44, J12.47, J12.48, J12.51, J12.52, J12.55, J12.56
- net Out_A5_Cube_2 is gone; now on net Ch_10_A1: J11.25
- net Out_E5_Cube_2 is gone; now on net Ch_52_A1: J11.22
- net Out_E6_Cube_2 is gone; now on net Ch_32_A1: J11.34
- net Out_E7_Cube_2 is gone; now on net Ch_62_A1: J11.02
- net Out_E8_Cube_2 is gone; now on net Ch_38_A1: J11.01
- net Out_F3_Cube_2 is gone; now on net Ch_04_A1: J11.33
- net Out_F5_Cube_2 is gone; now on net Ch_50_A1: J11.18
- net Out_F6_Cube_2 is gone; now on net Ch_58_A1: J11.14
- net Out_F7_Cube_2 is gone; now on net Ch_56_A1: J11.10
- net Out_F8_Cube_2 is gone; now on net Ch_18_A1: J11.17
- net Out_G2_Cube_2 is gone; now on net Ch_02_A1: J11.29
- net Out_G5_Cube_2 is gone; now on net Ch_42_A1: J11.26
- net Out_G6_Cube_2 is gone; now on net Ch_46_A1: J11.30
- net Out_G7_Cube_2 is gone; now on net Ch_12_A1: J11.13
- net Out_G8_Cube_2 is gone; now on net Ch_28_A1: J11.09
- net Out_H5_Cube_2 is gone; now on net Ch_06_A1: J11.21
- net Out_H7_Cube_2 is gone; now on net Ch_22_A1: J11.05
- net Out_H8_Cube_2 is gone; now on net Ch_64_A1: J11.06
- net +3.3_1V: now also TP2.1
- net +3.3_2V: now also TP3.1
- net +3.3_3V: now also TP4.1
- net +3.3_4V: now also TP5.1
- net 1V1_A1: now also TP1.1
- now unconnected: J2.06, J2.08, J2.10, J2.12, J2.14, J4.06, J4.08, J4.10, J4.12, J4.14, J6.06, J6.08, J6.10, J6.12, J6.14, J8.06, J8.08, J8.10, J8.12, J8.14
- no-connect marks 20 -> 36

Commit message: .
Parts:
- added GND1: GND, TestPoint:TestPoint_Pad_1.0x1.0mm, symbol Connector:TestPoint
- added TP10: HV_5, TestPoint:TestPoint_Pad_1.0x1.0mm, symbol Connector:TestPoint
- added TP11: HV_6, TestPoint:TestPoint_Pad_1.0x1.0mm, symbol Connector:TestPoint
- added TP12: HV_7, TestPoint:TestPoint_Pad_1.0x1.0mm, symbol Connector:TestPoint
- added TP13: HV_8, TestPoint:TestPoint_Pad_1.0x1.0mm, symbol Connector:TestPoint
- added TP6: HV_1, TestPoint:TestPoint_Pad_1.0x1.0mm, symbol Connector:TestPoint
- added TP7: HV_2, TestPoint:TestPoint_Pad_1.0x1.0mm, symbol Connector:TestPoint
- added TP8: HV_3, TestPoint:TestPoint_Pad_1.0x1.0mm, symbol Connector:TestPoint
- added TP9: HV_4, TestPoint:TestPoint_Pad_1.0x1.0mm, symbol Connector:TestPoint
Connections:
- net Out_A5_Cube_1 is gone; now on net Ch_05_A1: J9.25
- net Out_E1_Cube_1 is gone; now on net Ch_37_A1: J9.38
- net Out_E2_Cube_1 is gone; now on net Ch_57_A1: J9.50
- net Out_E3_Cube_1 is gone; now on net Ch_47_A1: J9.46
- net Out_E4_Cube_1 is gone; now on net Ch_09_A1: J9.37
- net Out_E5_Cube_1 is gone; now on net Ch_39_A1: J9.22
- net Out_E6_Cube_1 is gone; now on net Ch_43_A1: J9.34
- net Out_E7_Cube_1 is gone; now on net Ch_59_A1: J9.02
- net Out_E8_Cube_1 is gone; now on net Ch_31_A1: J9.01
- net Out_F1_Cube_1 is gone; now on net Ch_63_A1: J9.58
- net Out_F2_Cube_1 is gone; now on net Ch_61_A1: J9.60
- net Out_F3_Cube_1 is gone; now on net Ch_01_A1: J9.33
- net Out_F4_Cube_1 is gone; now on net Ch_53_A1: J9.42
- net Out_F5_Cube_1 is gone; now on net Ch_41_A1: J9.18
- net Out_F6_Cube_1 is gone; now on net Ch_45_A1: J9.14
- net Out_F7_Cube_1 is gone; now on net Ch_49_A1: J9.10
- net Out_F8_Cube_1 is gone; now on net Ch_19_A1: J9.17
- net Out_G1_Cube_1 is gone; now on net Ch_55_A1: J9.54
- net Out_G2_Cube_1 is gone; now on net Ch_03_A1: J9.29
- net Out_G3_Cube_1 is gone; now on net Ch_17_A1: J9.57
- net Out_G4_Cube_1 is gone; now on net Ch_15_A1: J9.45
- net Out_G5_Cube_1 is gone; now on net Ch_35_A1: J9.26
- net Out_G6_Cube_1 is gone; now on net Ch_27_A1: J9.30
- net Out_G7_Cube_1 is gone; now on net Ch_21_A1: J9.13
- net Out_G8_Cube_1 is gone; now on net Ch_25_A1: J9.09
- net Out_H1_Cube_1 is gone; now on net Ch_11_A1: J9.49
- net Out_H2_Cube_1 is gone; now on net Ch_23_A1: J9.53
- net Out_H3_Cube_1 is gone; now on net Ch_07_A1: J9.41
- net Out_H4_Cube_1 is gone; now on net Ch_33_A1: J9.59
- net Out_H5_Cube_1 is gone; now on net Ch_13_A1: J9.21
- net Out_H7_Cube_1 is gone; now on net Ch_29_A1: J9.05
- net Out_H8_Cube_1 is gone; now on net Ch_51_A1: J9.06
- net GND: now also GND1.1
- net HV_1-32_A1: now also J19.30 (Pin_30), TP12.1; no longer J19.26 (Pin_26)
- net HV_1-32_A2: now also J19.26 (Pin_26), TP10.1; no longer J19.28 (Pin_28)
- net HV_1-32_A3: now also J19.22 (Pin_22), TP8.1; no longer J19.30 (Pin_30)
- net HV_1-32_A4: now also J19.18 (Pin_18), TP6.1; no longer J19.32 (Pin_32)
- net HV_33-64_A1: now also J19.32 (Pin_32), TP13.1; no longer J19.24 (Pin_24)
- net HV_33-64_A2: now also J19.28 (Pin_28), TP11.1; no longer J19.22 (Pin_22)
- net HV_33-64_A3: now also J19.24 (Pin_24), TP9.1; no longer J19.20 (Pin_20)
- net HV_33-64_A4: now also J19.20 (Pin_20), TP7.1; no longer J19.18 (Pin_18)
